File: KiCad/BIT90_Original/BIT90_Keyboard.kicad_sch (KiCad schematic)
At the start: 65 parts, among them SW1 MINUS, SW10 8, SW11 4, SW12 BS, SW13 DEL, SW14 2, SW15 6, SW16 ZERO, SW17 P, SW18 Y, SW19 W, SW2 7, SW20 ], SW21 UP, SW22 ESC, SW23 R, SW24 I, SW25 [, SW26 U, SW27 E, SW28 RUBOUT, SW29 RIGHT, SW3 3, SW30 Q, SW31 T, SW32 O, SW33 SEMICOLON, SW34 H, SW35 S, SW36 @, SW37 FWDSLASH, SW38 CAPS/LOWER, SW39 F, SW4 BACKSLASH, SW40 K, SW41 COLON, SW42 J, SW43 D, SW44 CR, SW45 PERIOD, SW46 A, SW47 G, SW48 L, SW49 N, SW5 INS, SW50 V, SW51 X, SW52 M, SW53 COMMA, SW54 Z, SW55 C, SW56 B, SW57 SHIFT, SW58 BIT, SW59 BASIC, SW6 1, SW60 LEFT, SW61 DOWN, SW62 CTRL, SW63 SPACE, SW64 FCTN, SW65 RST, SW7 5, SW8 6, SW9 CARAT

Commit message: Added "Processor" Sheet 6-1
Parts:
- removed SW65: RST, symbol Switch:SW_Push_45deg
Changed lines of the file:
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@@
-	(wire
-		(pts
-			(xy 228.6 33.02) (xy 236.22 33.02)
-		)
-		(stroke
-			(width 0)
-			(type default)
-		)
-	)
 	(wire
 		(pts
@@
 		(pts
 			(xy 171.45 69.85) (xy 190.5 69.85)
-		)
-		(stroke
-			(width 0)
-			(type default)
-		)
-	)
-	(wire
-		(pts
-			(xy 246.38 38.1) (xy 241.3 38.1)
 		)
 		(stroke
@@
 		)
 	)
-	(global_label "+5V"
-		(shape input)
-		(at 228.6 33.02 180)
+	(global_label "KI_{2}"
+		(shape output)
+		(at 83.82 148.59 270)
 		(fields_autoplaced yes)
 		(effects
@@
 		)
 		(property "Intersheetrefs" "${INTERSHEET_REFS}"
-			(at 221.7443 33.02 0)
+			(at 83.82 154.4684 90)
 			(effects
 				(font
@@
 		)
 	)
-	(global_label "KI_{2}"
+	(global_label "KI_{7}"
 		(shape output)
-		(at 83.82 148.59 270)
+		(at 166.37 148.59 270)
 		(fields_autoplaced yes)
 		(effects
@@
 		)
 		(property "Intersheetrefs" "${INTERSHEET_REFS}"
-			(at 83.82 154.4684 90)
+			(at 166.37 154.4684 90)
 			(effects
 				(font
@@
 		)
 	)
-	(global_label "KI_{7}"
-		(shape output)
-		(at 166.37 148.59 270)
+	(global_label "KO_{0}"
+		(shape input)
+		(at 190.5 39.37 0)
 		(fields_autoplaced yes)
 		(effects
@@
 				(size 1.27 1.27)
 			)
-			(justify right)
+			(justify left)
 		)
 		(property "Intersheetrefs" "${INTERSHEET_REFS}"
-			(at 166.37 154.4684 90)
-			(effects
-				(font
-					(size 1.27 1.27)
-				)
-				(justify right)
-				(hide yes)
-			)
-		)
-	)
-	(global_label "KO_{0}"
+			(at 197.1041 39.37 0)
+			(effects
+				(font
+					(size 1.27 1.27)
+				)
+				(justify left)
+				(hide yes)
+			)
+		)
+	)
+	(global_label "KO_{7}"
 		(shape input)
-		(at 190.5 39.37 0)
+		(at 190.5 140.97 0)
 		(fields_autoplaced yes)
 		(effects
@@
 		)
 		(property "Intersheetrefs" "${INTERSHEET_REFS}"
-			(at 197.1041 39.37 0)
+			(at 197.1041 140.97 0)
 			(effects
 				(font
@@
 		)
 	)
-	(global_label "KO_{7}"
-		(shape input)
-		(at 190.5 140.97 0)
+	(global_label "KI_{0}"
+		(shape output)
+		(at 50.8 148.59 270)
 		(fields_autoplaced yes)
 		(effects
@@
 				(size 1.27 1.27)
 			)
-			(justify left)
+			(justify right)
 		)
 		(property "Intersheetrefs" "${INTERSHEET_REFS}"
-			(at 197.1041 140.97 0)
-			(effects
-				(font
-					(size 1.27 1.27)
-				)
-				(justify left)
-				(hide yes)
-			)
-		)
-	)
-	(global_label "KI_{0}"
+			(at 50.8 154.4684 90)
+			(effects
+				(font
+					(size 1.27 1.27)
+				)
+				(justify right)
+				(hide yes)
+			)
+		)
+	)
+	(global_label "KI_{3}"
 		(shape output)
-		(at 50.8 148.59 270)
+		(at 100.33 148.59 270)
 		(fields_autoplaced yes)
 		(effects
@@
 		)
 		(property "Intersheetrefs" "${INTERSHEET_REFS}"
-			(at 50.8 154.4684 90)
+			(at 100.33 154.4684 90)
 			(effects
 				(font
@@
 		)
 	)
-	(global_label "KI_{3}"
+	(global_label "KI_{1}"
 		(shape output)
-		(at 100.33 148.59 270)
+		(at 67.31 148.59 270)
 		(fields_autoplaced yes)
 		(effects
@@
 		)
 		(property "Intersheetrefs" "${INTERSHEET_REFS}"
-			(at 100.33 154.4684 90)
+			(at 67.31 154.4684 90)
 			(effects
 				(font
@@
 		)
 	)
-	(global_label "KI_{1}"
+	(global_label "KI_{5}"
 		(shape output)
-		(at 67.31 148.59 270)
+		(at 133.35 148.59 270)
 		(fields_autoplaced yes)
 		(effects
@@
 		)
 		(property "Intersheetrefs" "${INTERSHEET_REFS}"
-			(at 67.31 154.4684 90)
+			(at 133.35 154.4684 90)
 			(effects
 				(font
@@
 		)
 	)
-	(global_label "KI_{5}"
-		(shape output)
-		(at 133.35 148.59 270)
+	(global_label "KO_{2}"
+		(shape input)
+		(at 190.5 69.85 0)
 		(fields_autoplaced yes)
 		(effects
@@
 				(size 1.27 1.27)
 			)
-			(justify right)
+			(justify left)
 		)
 		(property "Intersheetrefs" "${INTERSHEET_REFS}"
-			(at 133.35 154.4684 90)
-			(effects
-				(font
-					(size 1.27 1.27)
-				)
-				(justify right)
-				(hide yes)
-			)
-		)
-	)
-	(global_label "KO_{2}"
+			(at 197.1041 69.85 0)
+			(effects
+				(font
+					(size 1.27 1.27)
+				)
+				(justify left)
+				(hide yes)
+			)
+		)
+	)
+	(global_label "KO_{5}"
 		(shape input)
-		(at 190.5 69.85 0)
+		(at 190.5 113.03 0)
 		(fields_autoplaced yes)
 		(effects
@@
 		)
 		(property "Intersheetrefs" "${INTERSHEET_REFS}"
-			(at 197.1041 69.85 0)
+			(at 197.1041 113.03 0)
 			(effects
 				(font
@@
 		)
 	)
-	(global_label "KO_{5}"
+	(global_label "KO_{1}"
 		(shape input)
-		(at 190.5 113.03 0)
+		(at 190.5 54.61 0)
 		(fields_autoplaced yes)
 		(effects
@@
 		)
 		(property "Intersheetrefs" "${INTERSHEET_REFS}"
-			(at 197.1041 113.03 0)
-			(effects
-				(font
-					(size 1.27 1.27)
-				)
-				(justify left)
-				(hide yes)
-			)
-		)
-	)
-	(global_label "KO_{1}"
-		(shape input)
-		(at 190.5 54.61 0)
-		(fields_autoplaced yes)
-		(effects
-			(font
-				(size 1.27 1.27)
-			)
-			(justify left)
-		)
-		(property "Intersheetrefs" "${INTERSHEET_REFS}"
 			(at 197.1041 54.61 0)
-			(effects
-				(font
-					(size 1.27 1.27)
-				)
-				(justify left)
-				(hide yes)
-			)
-		)
-	)
-	(global_label "RST"
-		(shape output)
-		(at 246.38 38.1 0)
-		(fields_autoplaced yes)
-		(effects
-			(font
-				(size 1.27 1.27)
-			)
-			(justify left)
-		)
-		(property "Intersheetrefs" "${INTERSHEET_REFS}"
-			(at 252.8123 38.1 0)
 			(effects
 				(font
@@
 					(unit 1)
 				)
-			)
-		)
-	)
-	(symbol
-		(lib_id "Switch:SW_Push_45deg")
-		(at 238.76 35.56 0)
-		(unit 1)
-		(exclude_from_sim no)
-		(in_bom yes)
-		(on_board yes)
-		(dnp no)
-		(fields_autoplaced yes)
-		(property "Reference" "SW65"
-			(at 238.76 27.94 0)
-			(effects
-				(font
-					(size 1.27 1.27)
-				)
-			)
-		)
-		(property "Value" "RST"
-			(at 238.76 30.48 0)
-			(effects
-				(font
-					(size 1.27 1.27)
-				)
-			)
-		)
-		(property "Footprint" ""
-			(at 238.76 35.56 0)
-			(effects
-				(font
-					(size 1.27 1.27)
-				)
-				(hide yes)
-			)
-		)
-		(property "Datasheet" "~"
-			(at 238.76 35.56 0)
-			(effects
-				(font
-					(size 1.27 1.27)
-				)
-				(hide yes)
-			)
-		)
-		(property "Description" "Push button switch, normally open, two pins, 45° tilted"
-			(at 238.76 35.56 0)
-			(effects
-				(font
-					(size 1.27 1.27)
-				)
-				(hide yes)
-			)
-		)
-		(pin "2"
-		)
-		(pin "1"
-		)
-		(instances
-			(project "BIT90_Original"
-				(path "/d65498c3-6385-4920-ac0f-4c76daf90780/7004f5d0-9464-4578-a2ed-1d5ed8c6edba"
-					(reference "SW65")
-					(unit 1)
-				)

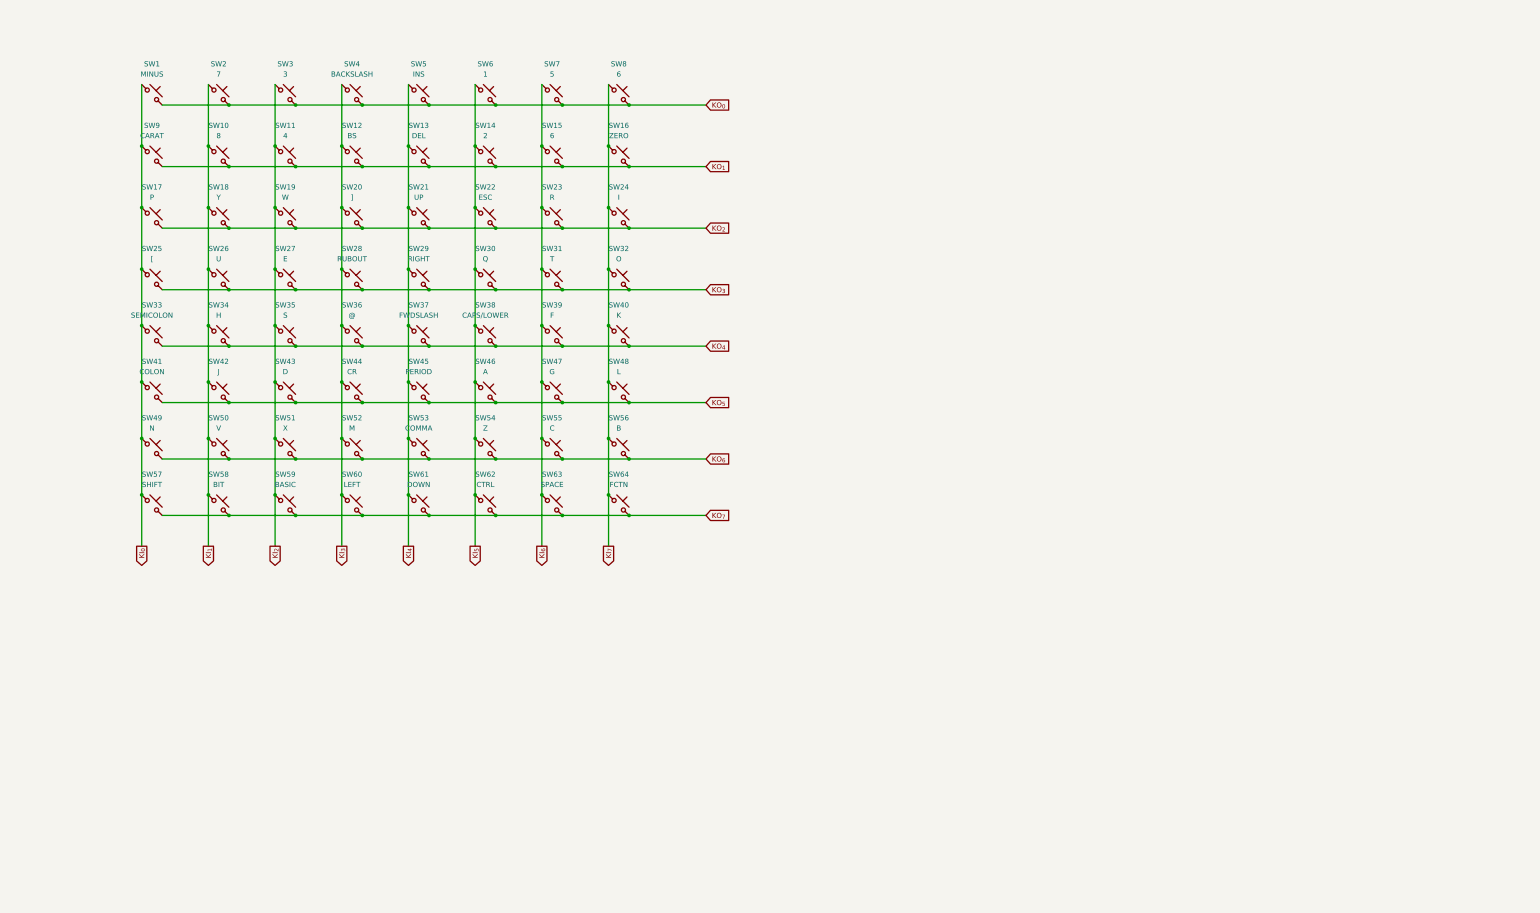
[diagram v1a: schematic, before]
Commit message: Completed keyboard schematic
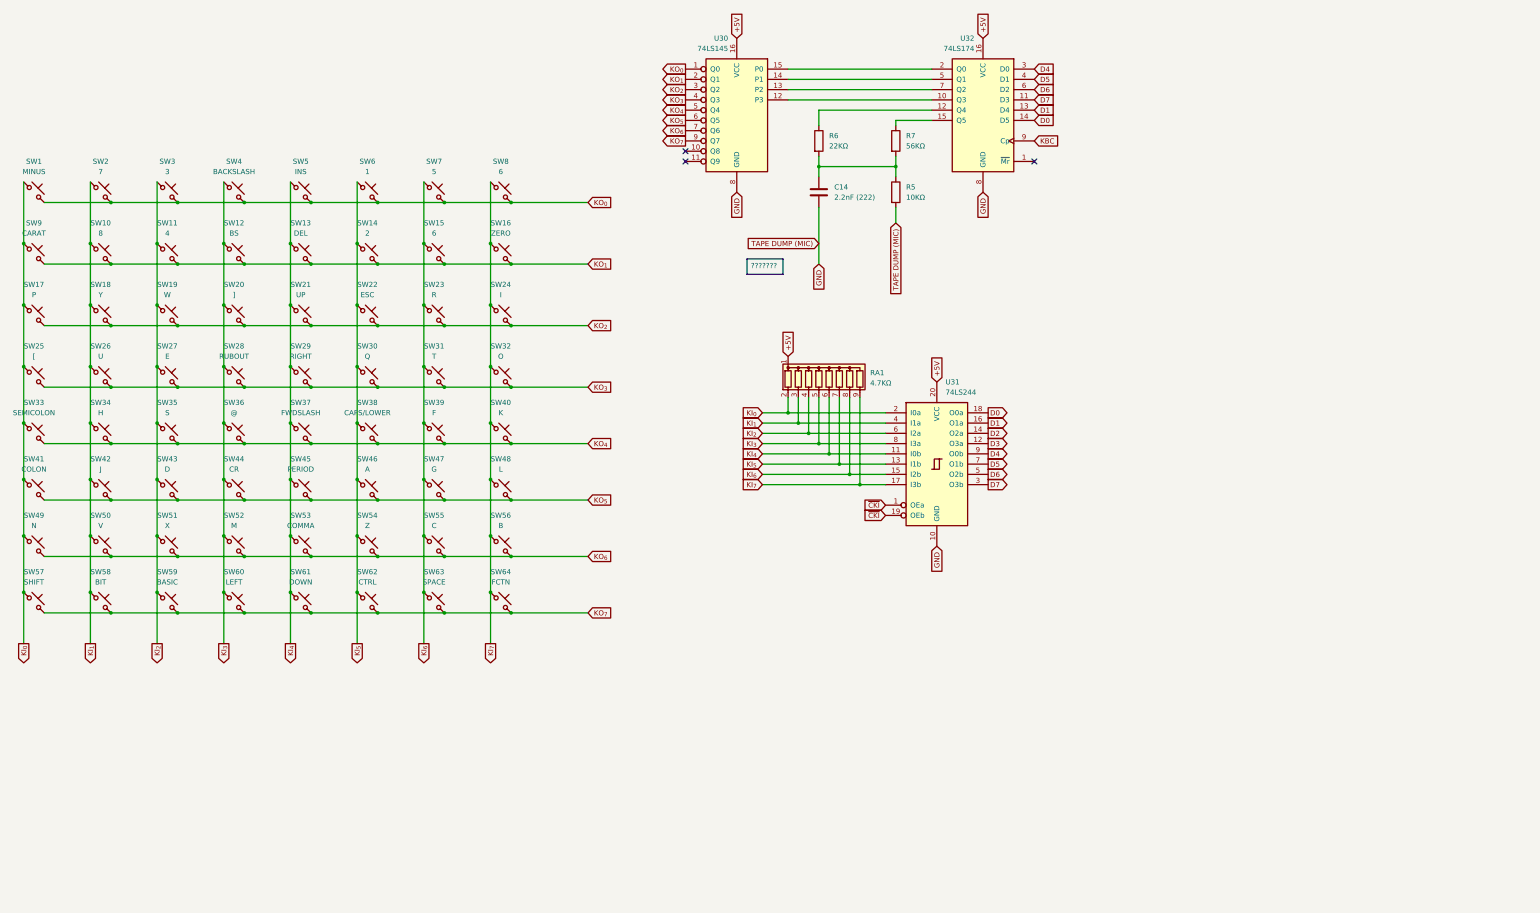
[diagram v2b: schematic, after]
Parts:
- added C14: 2.2nF (222), symbol Device:C
- added R5: 10KΩ, symbol Device:R
- added R6: 22KΩ, symbol Device:R
- added R7: 56KΩ, symbol Device:R
- added RA1: 4.7KΩ, Resistor_THT:R_Array_SIP9, symbol Device:R_Network08
- added U30: 74LS145, symbol 74xx:74LS145
- added U31: 74LS244, symbol 74xx:74LS244
- added U32: 74LS174, symbol 74xx:74LS174
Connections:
- net KI_{0}: now also RA1.2 (R1), U31.2 (I0a)
- net KI_{1}: now also RA1.3 (R2), U31.4 (I1a)
- net KI_{2}: now also RA1.4 (R3), U31.6 (I2a)
- net KI_{3}: now also RA1.5 (R4), U31.8 (I3a)
- net KI_{4}: now also RA1.6 (R5), U31.11 (I0b)
- net KI_{5}: now also RA1.7 (R6), U31.13 (I1b)
- net KI_{6}: now also RA1.8 (R7), U31.15 (I2b)
- net KI_{7}: now also RA1.9 (R8), U31.17 (I3b)
- net KO_{0}: now also U30.1 (Q0)
- net KO_{1}: now also U30.2 (Q1)
- net KO_{2}: now also U30.3 (Q2)
- net KO_{3}: now also U30.4 (Q3)
- net KO_{4}: now also U30.5 (Q4)
- net KO_{5}: now also U30.6 (Q5)
- net KO_{6}: now also U30.7 (Q6)
- net KO_{7}: now also U30.9 (Q7)
- new net: R6.1, U32.12 (Q4)
- new net: C14.1, R5.1, R6.2, R7.2
- new net: U30.12 (P3), U32.10 (Q3)
- new net: R7.1, U32.15 (Q5)
- new net: U30.15 (P0), U32.2 (Q0)
- new net: U30.14 (P1), U32.5 (Q1)
- new net: U30.13 (P2), U32.7 (Q2)
- new net +5V: RA1.1 (common), U30.16 (VCC), U31.20 (VCC), U32.16 (VCC)
- new net D0: U31.18 (O0a), U32.14 (D5)
- new net D1: U31.16 (O1a), U32.13 (D4)
- new net D2: U31.14 (O2a)
- new net D3: U31.12 (O3a)
- new net D4: U31.9 (O0b), U32.3 (D0)
- new net D5: U31.7 (O1b), U32.4 (D1)
- new net D6: U31.5 (O2b), U32.6 (D2)
- new net D7: U31.3 (O3b), U32.11 (D3)
- new net GND: C14.2, R5.2, U30.8 (GND), U31.10 (GND), U32.8 (GND)
- new net KBC: U32.9 (Cp)
- new net ~{CKI}: U31.1 (OEa), U31.19 (OEb)
- no-connect marks 0 -> 3
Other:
- moved on the sheet: SW1, SW10, SW11, SW12, SW13, SW14, SW15, SW16, SW17, SW18, SW19, SW2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

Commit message: Added "Video Control" schematic
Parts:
- SW36: value @ -> AT

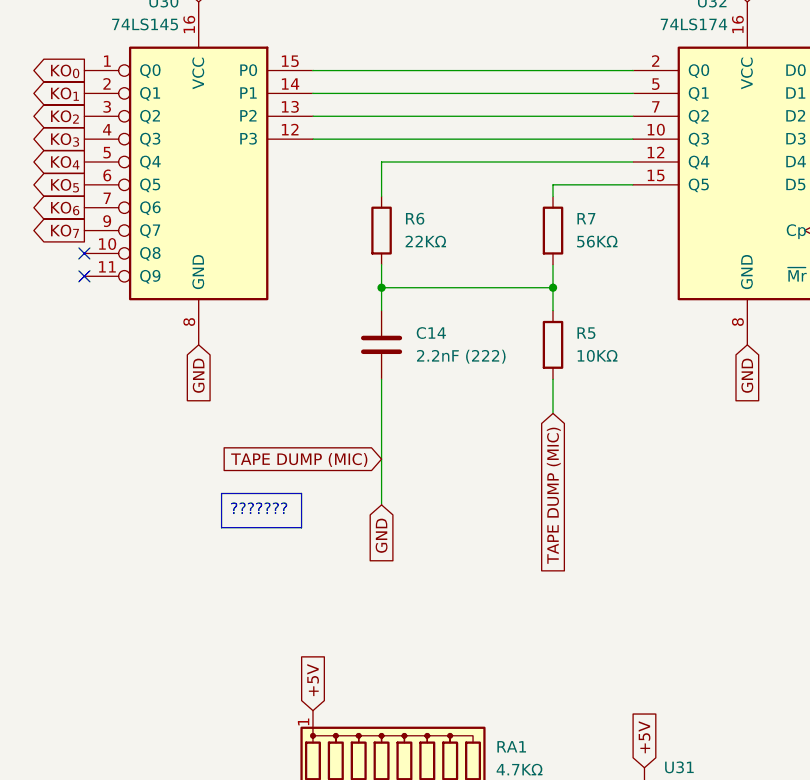
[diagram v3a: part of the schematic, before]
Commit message: Added "Joystick, Audio, Tape Out" schematic
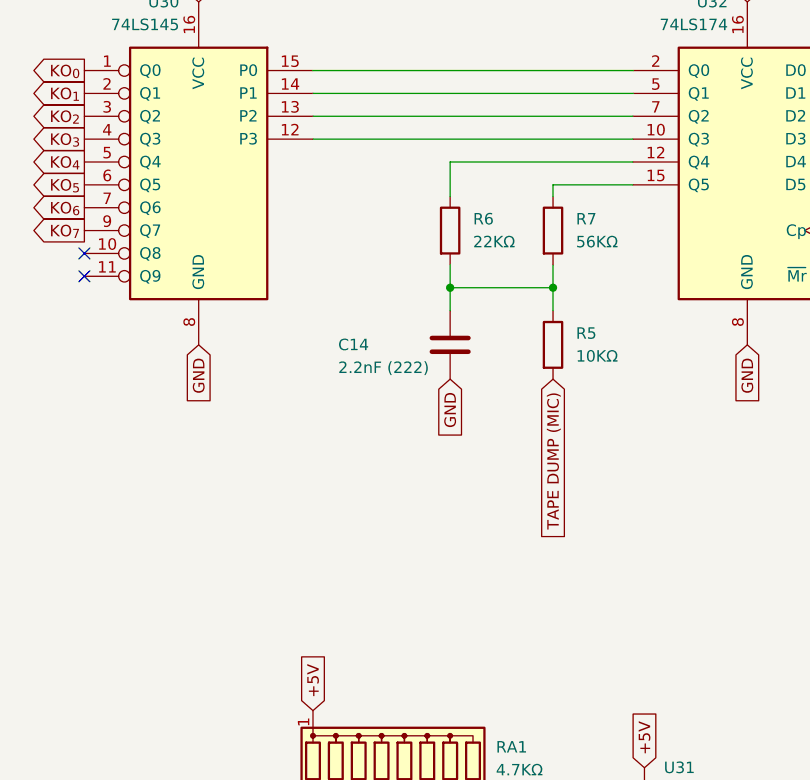
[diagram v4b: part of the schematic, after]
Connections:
- net GND: no longer R5.2
- new net TAPE DUMP (MIC): R5.2
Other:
- moved on the sheet: C14, R6
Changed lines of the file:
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@@
 		(comment 4 "Based on original schematics from BIT Corporation")
 	)
-	(text_box "???????"
-		(exclude_from_sim no)
-		(at 200.66 77.47 0)
-		(size 8.89 3.81)
-		(margins 0.9525 0.9525 0.9525 0.9525)
-		(stroke
-			(width 0)
-			(type solid)
-		)
-		(fill
-			(type none)
-		)
-		(effects
-			(font
-				(size 1.27 1.27)
-			)
-			(justify left top)
-		)
-	)
 	(junction
 		(at 87.63 132.08)
@@
 	)
 	(junction
-		(at 218.44 54.61)
+		(at 226.06 54.61)
 		(diameter 0)
 		(color 0 0 0 0)
@@
 	(wire
 		(pts
-			(xy 246.38 40.64) (xy 218.44 40.64)
+			(xy 246.38 40.64) (xy 226.06 40.64)
 		)
 		(stroke
@@
 	(wire
 		(pts
-			(xy 218.44 54.61) (xy 218.44 52.07)
+			(xy 226.06 54.61) (xy 226.06 52.07)
 		)
 		(stroke
@@
 	(wire
 		(pts
-			(xy 218.44 54.61) (xy 237.49 54.61)
+			(xy 226.06 54.61) (xy 237.49 54.61)
 		)
 		(stroke
@@
 	(wire
 		(pts
-			(xy 218.44 78.74) (xy 218.44 64.77)
-		)
-		(stroke
-			(width 0)
-			(type default)
-		)
-	)
-	(wire
-		(pts
 			(xy 43.18 151.13) (xy 59.69 151.13)
 		)
@@
 	(wire
 		(pts
-			(xy 218.44 57.15) (xy 218.44 54.61)
+			(xy 226.06 57.15) (xy 226.06 54.61)
 		)
 		(stroke
@@
 	(wire
 		(pts
-			(xy 218.44 40.64) (xy 218.44 44.45)
+			(xy 226.06 40.64) (xy 226.06 44.45)
 		)
 		(stroke
@@
 	(wire
 		(pts
-			(xy 237.49 68.58) (xy 237.49 64.77)
-		)
-		(stroke
-			(width 0)
-			(type default)
-		)
-	)
-	(wire
-		(pts
 			(xy 204.47 123.19) (xy 218.44 123.19)
 		)
@@
 	(global_label "TAPE DUMP (MIC)"
 		(shape input)
-		(at 237.49 68.58 270)
+		(at 237.49 64.77 270)
 		(fields_autoplaced yes)
 		(effects
@@
 		)
 		(property "Intersheetrefs" "${INTERSHEET_REFS}"
-			(at 237.49 88.3171 90)
+			(at 237.49 84.5071 90)
 			(effects
 				(font
@@
 		)
 	)
-	(global_label "TAPE DUMP (MIC)"
-		(shape input)
-		(at 218.44 73.66 180)
-		(fields_autoplaced yes)
-		(effects
-			(font
-				(size 1.27 1.27)
-			)
-			(justify right)
-		)
-		(property "Intersheetrefs" "${INTERSHEET_REFS}"
-			(at 198.7029 73.66 0)
-			(effects
-				(font
-					(size 1.27 1.27)
-				)
-				(justify right)
-				(hide yes)
-			)
-		)
-	)
 	(global_label "+5V"
 		(shape input)
@@
 	(global_label "GND"
 		(shape input)
-		(at 218.44 78.74 270)
+		(at 226.06 64.77 270)
 		(fields_autoplaced yes)
 		(effects
@@
 		)
 		(property "Intersheetrefs" "${INTERSHEET_REFS}"
-			(at 218.44 85.5957 90)
+			(at 226.06 71.6257 90)
 			(effects
 				(font
@@
 	(symbol
 		(lib_id "Device:R")
-		(at 218.44 48.26 0)
+		(at 226.06 48.26 0)
 		(unit 1)
 		(exclude_from_sim no)
@@
 		(fields_autoplaced yes)
 		(property "Reference" "R6"
-			(at 220.98 46.9899 0)
+			(at 228.6 46.9899 0)
 			(effects
 				(font
@@
 		)
 		(property "Value" "22KΩ"
-			(at 220.98 49.5299 0)
+			(at 228.6 49.5299 0)
 			(effects
 				(font
@@
 		)
 		(property "Footprint" ""
-			(at 216.662 48.26 90)
+			(at 224.282 48.26 90)
 			(effects
 				(font
@@
 		)
 		(property "Datasheet" "~"
-			(at 218.44 48.26 0)
+			(at 226.06 48.26 0)
 			(effects
 				(font
@@
 		)
 		(property "Description" "Resistor"
-			(at 218.44 48.26 0)
+			(at 226.06 48.26 0)
 			(effects
 				(font
@@
 	(symbol
 		(lib_id "Device:C")
-		(at 218.44 60.96 0)
+		(at 226.06 60.96 0)
 		(unit 1)
 		(exclude_from_sim no)
@@
 		(on_board yes)
 		(dnp no)
-		(fields_autoplaced yes)
 		(property "Reference" "C14"
-			(at 222.25 59.6899 0)
+			(at 213.614 60.96 0)
 			(effects
 				(font
@@
 		)
 		(property "Value" "2.2nF (222)"
-			(at 222.25 62.2299 0)
+			(at 213.614 63.5 0)
 			(effects
 				(font
@@
 		)
 		(property "Footprint" ""
-			(at 219.4052 64.77 0)
+			(at 227.0252 64.77 0)
 			(effects
 				(font
@@
 		)
 		(property "Datasheet" "~"
-			(at 218.44 60.96 0)
+			(at 226.06 60.96 0)
 			(effects
 				(font
@@
 		)
 		(property "Description" "Unpolarized capacitor"
-			(at 218.44 60.96 0)
+			(at 226.06 60.96 0)
 			(effects
 				(font
